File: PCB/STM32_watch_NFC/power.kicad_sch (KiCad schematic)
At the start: 26 parts, among them P1 USB_C_Plug_USB2.0, Q2 AO3400A, U4 LP5912-3.3DRV, U5 MCP73831-3-OT, U6 MT3608

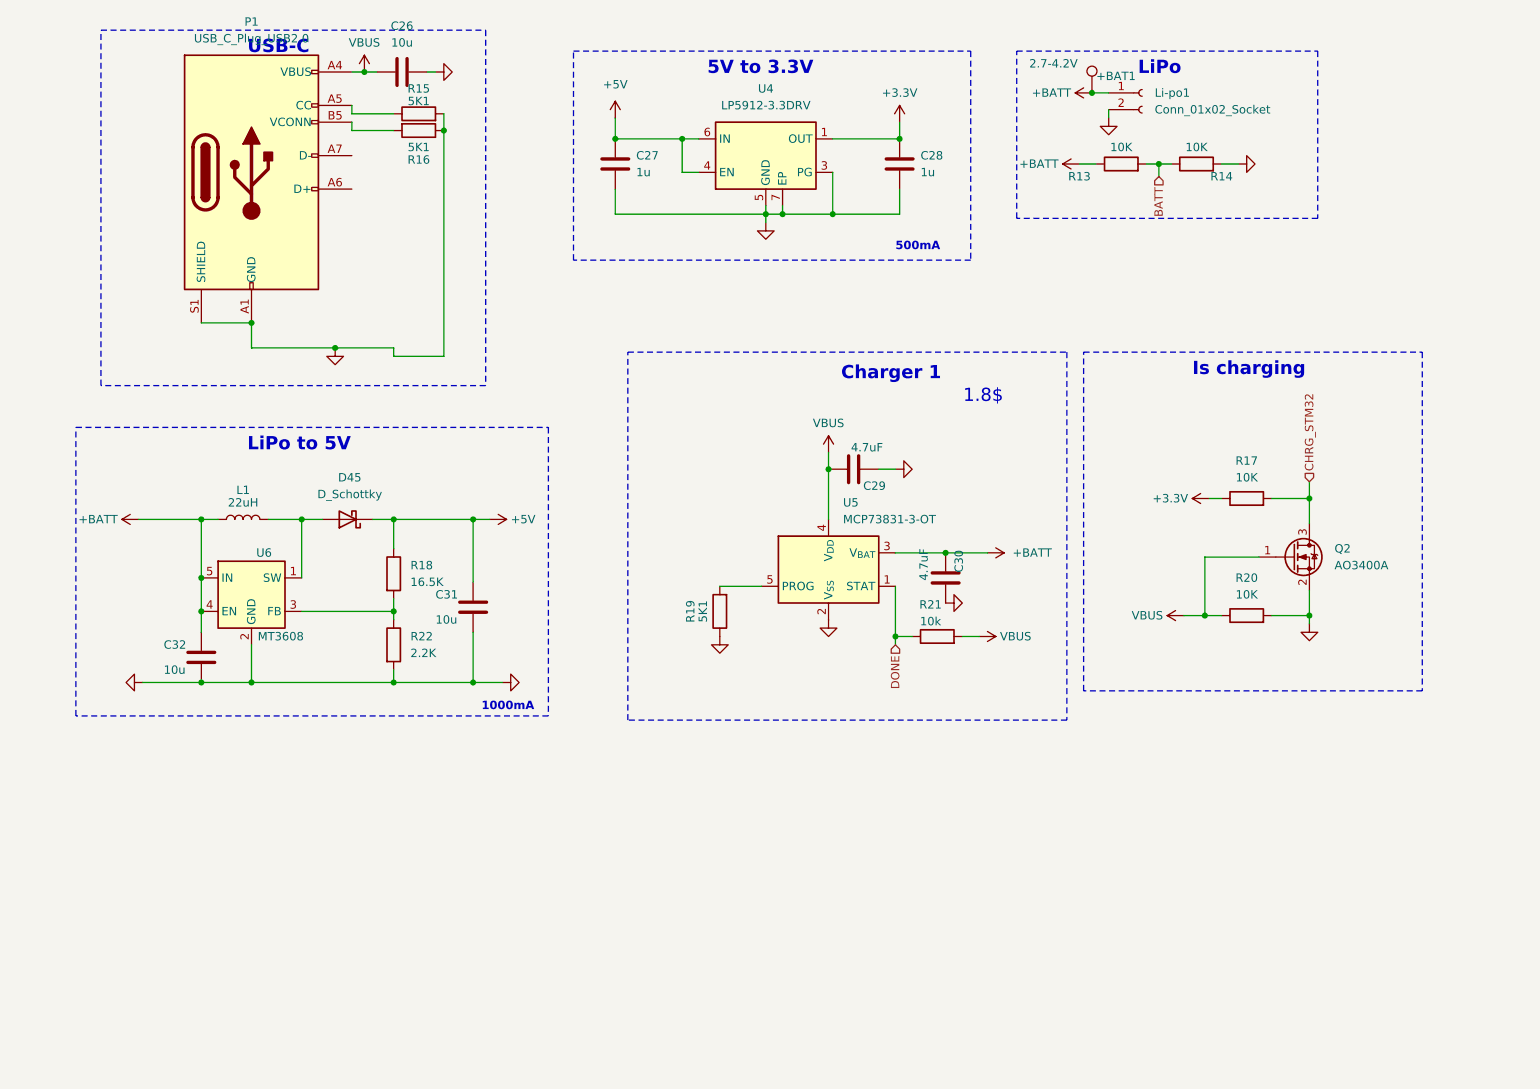
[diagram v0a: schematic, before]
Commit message: Whole power schema
I draw the whole power section and I am starting to create accelerometer with gyro
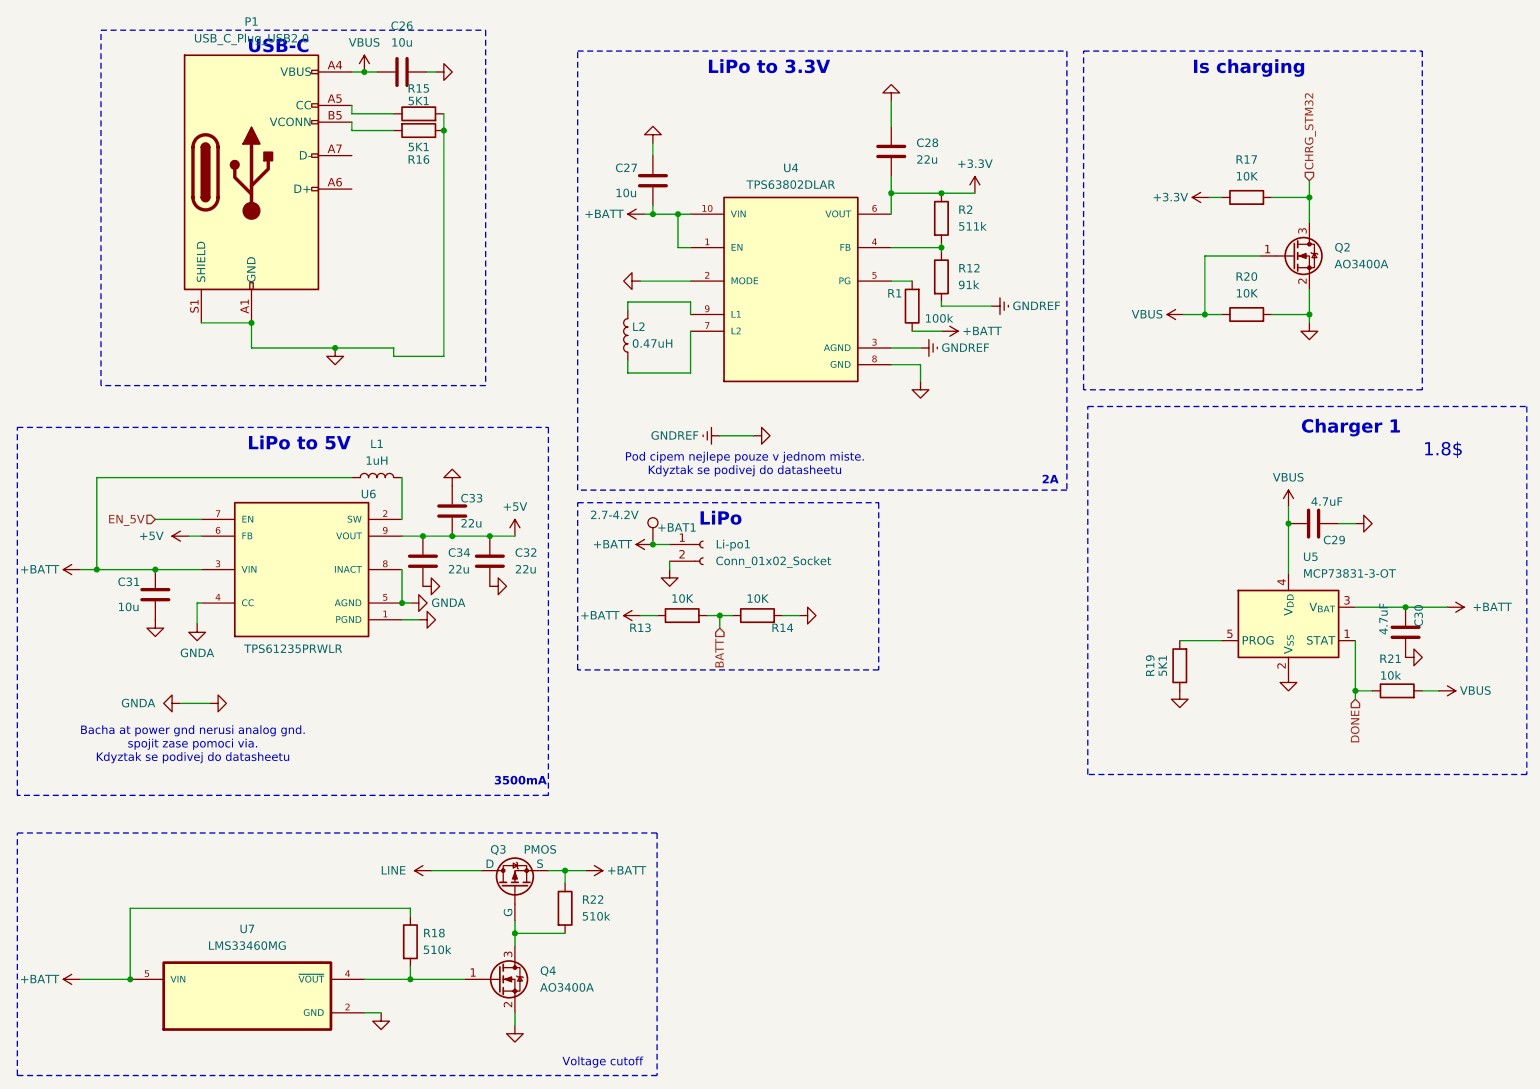
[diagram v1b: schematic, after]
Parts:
- removed D45: D_Schottky, Diode_SMD:D_SOD-523, symbol Device:D_Schottky
- removed U4: LP5912-3.3DRV, Package_SON:WSON-6-1EP_2x2mm_P0.65mm_EP1x1.6mm, symbol Regulator_Linear:LP5912-3.3DRV
- removed U6: MT3608, Package_TO_SOT_SMD:SOT-23-6, symbol Regulator_Switching:MT3608
- added C33, C34: 22u, symbol Device:C
- added L2: 0.47uH, symbol Device:L
- added Q3: PMOS, symbol Simulation_SPICE:PMOS
- added Q4: AO3400A, Package_TO_SOT_SMD:SOT-23, symbol Transistor_FET:AO3400A
- added R1: 100k, symbol Device:R
- added R12: 91k, symbol Device:R
- added R2: 511k, symbol Device:R
- added U4: TPS63802DLAR, TPS63802DLAR:VREG_TPS63802DLAR, symbol TPS63802DLAR:TPS63802DLAR
- added U6: TPS61235PRWLR, TPS61235PRWLR:CONV_TPS61235PRWLR, symbol TPS61235PRWLR:TPS61235PRWLR
- added U7: LMS33460MG, LMS33460MG:SOT65P210X110-5N, symbol LMS33460MG:LMS33460MG
- C27: value 1u -> 10u; footprint Capacitor_SMD:C_0402_1005Metric -> Capacitor_SMD:C_0603_1608Metric; LCSC C52923 -> C19702
- C28: value 1u -> 22u; footprint Capacitor_SMD:C_0402_1005Metric -> (none); LCSC C52923 -> (none)
- C32: value 10u -> 22u; footprint Capacitor_SMD:C_0603_1608Metric -> (none); LCSC C19702 -> (none)
- L1: value 22uH -> 1uH; footprint Inductor_SMD:L_Sunlord_SWPA3015S -> (none); LCSC C167761 -> (none)
- R18: value 16.5K -> 510k; footprint Resistor_SMD:R_0805_2012Metric -> (none); LCSC C104028 -> (none)
- R22: value 2.2K -> 510k; footprint Resistor_SMD:R_0402_1005Metric -> (none); LCSC C25879 -> (none)
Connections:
- net +3.3V: now also R2.1, U4.6 (VOUT)
- net +5V: now also C32.1, C33.2, C34.1, U6.6 (FB), U6.9 (VOUT); no longer C27.2, C31.1, R18.1
- net +BATT: now also C27.2, C31.1, R18.1, R22.1, Q3.3 (S), R1.1, U4.1 (EN), U4.10 (VIN), U6.3 (VIN), U7.5 (VIN); no longer C32.1
- net GND: now also C33.1, C34.2, Q4.2 (S), R12.2, U4.2 (MODE), U4.3 (AGND), U4.8 (GND), U6.1 (PGND), U6.4 (CC), U6.5 (AGND), U6.8 (INACT), U7.2 (GND), U7.3 (GND); no longer R22.2
- net at R18.2: now also Q4.1 (G), U7.4 (~{VOUT}); no longer R22.1
- net at L1.2: now also U6.2 (SW)
- new net: R12.1, R2.2, U4.4 (FB)
- new net: Q3.2 (G), Q4.3 (D), R22.2
- new net: L2.1, U4.7 (L2)
- new net: L2.2, U4.9 (L1)
- new net: R1.2, U4.5 (PG)
- new net EN_5V: U6.7 (EN)
- new net LINE: Q3.1 (D)
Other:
- note added: "2A"
- note added: "3500mA"
- note added: "Bacha at power gnd nerusi analog gnd. spojit zase pomoci via. Kdyztak se podivej do datasheetu"
- note added: "LiPo to 3.3V"
- note added: "Pod cipem nejlepe pouze v jednom miste. Kdyztak se podivej do datasheetu"
- note added: "Voltage cutoff"
- note removed: "1000mA"
- note removed: "500mA"
- note removed: "5V to 3.3V"
- moved on the sheet: +BAT1, C29, C30, Li-po1, Q2, R13, R14, R17, R19, R20, R21, U5

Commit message: Schema done
I redraw some footprints and added accelerometer with gyro
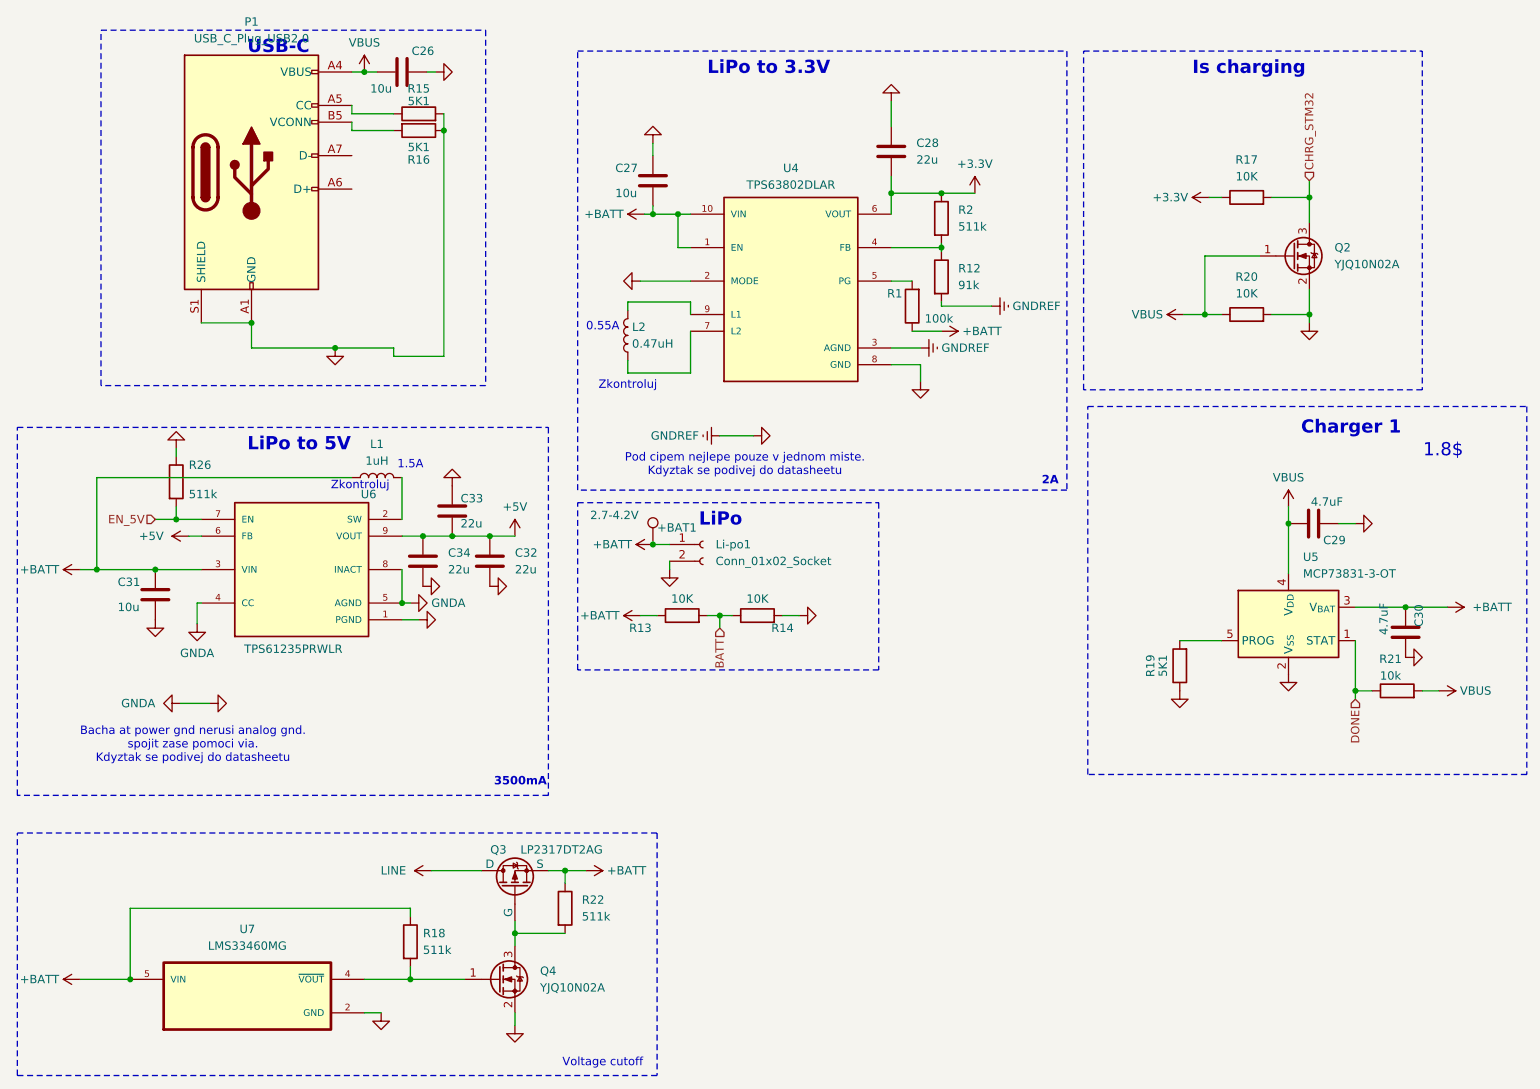
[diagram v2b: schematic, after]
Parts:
- added R26: 511k, Resistor_SMD:R_0603_1608Metric, symbol Device:R
- C28, C32, C33, C34: footprint (none) -> Capacitor_SMD:C_0603_1608Metric; LCSC (none) -> C59461
- L1: footprint (none) -> Inductor_SMD:L_1008_2520Metric; LCSC (none) -> C76795
- L2: footprint (none) -> Inductor_SMD:L_0805_2012Metric; LCSC (none) -> C370012
- Q2, Q4: value AO3400A -> YJQ10N02A; footprint Package_TO_SOT_SMD:SOT-23 -> Package_DFN_QFN:Diodes_UDFN2020-6_Type-F; LCSCv C344010 -> C919558
- Q3: value PMOS -> LP2317DT2AG; footprint (none) -> Package_DFN_QFN:Diodes_UDFN2020-6_Type-F; LCSC (none) -> C383254
- R1: footprint (none) -> Resistor_SMD:R_0603_1608Metric; LCSC (none) -> C25803
- R12: footprint (none) -> Resistor_SMD:R_0603_1608Metric; LCSC (none) -> C2907077
- R18, R22: value 510k -> 511k; footprint (none) -> Resistor_SMD:R_0603_1608Metric; LCSC (none) -> C2930114
- R2: footprint (none) -> Resistor_SMD:R_0603_1608Metric; LCSC (none) -> C2930114
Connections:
- net EN_5V: now also R26.2
- net GND: now also R26.1
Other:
- note added: "0.55A"
- note added: "1.5A"
- note added: "Zkontroluj"

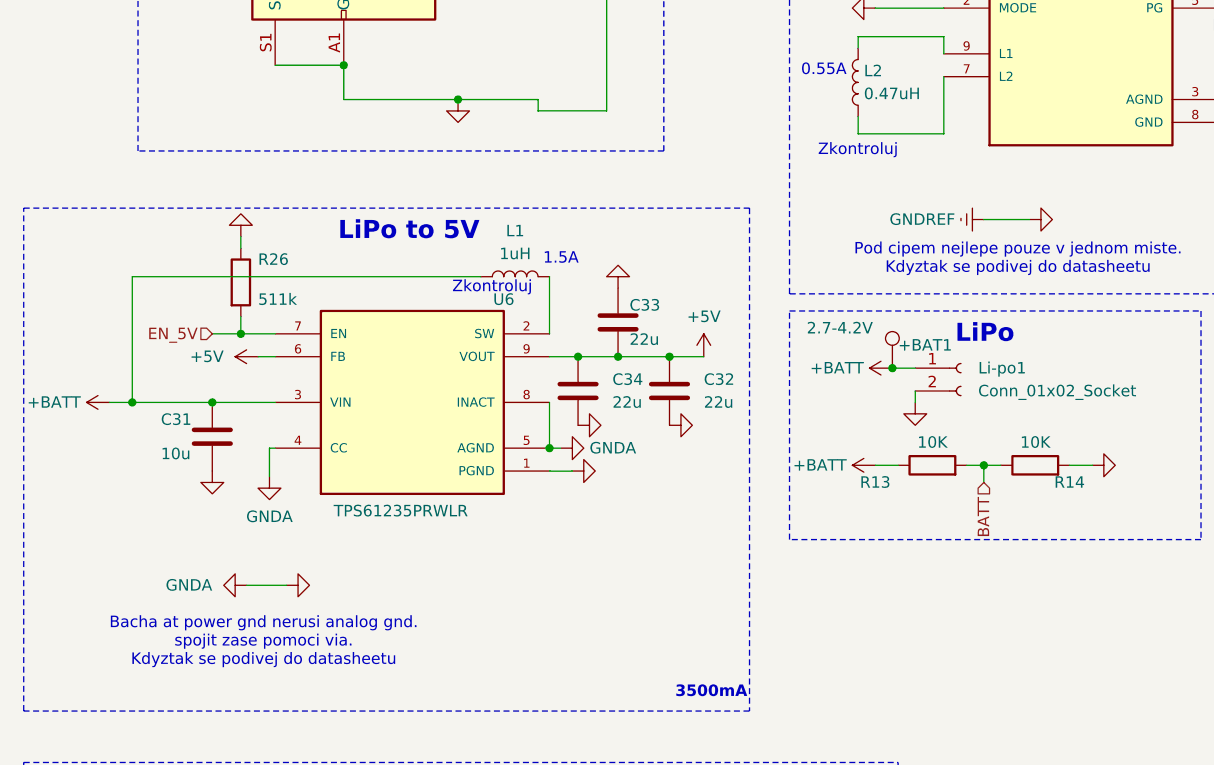
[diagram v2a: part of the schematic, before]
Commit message: PCB rev.B.1 #3
routing almost done - now checking and silkscreen
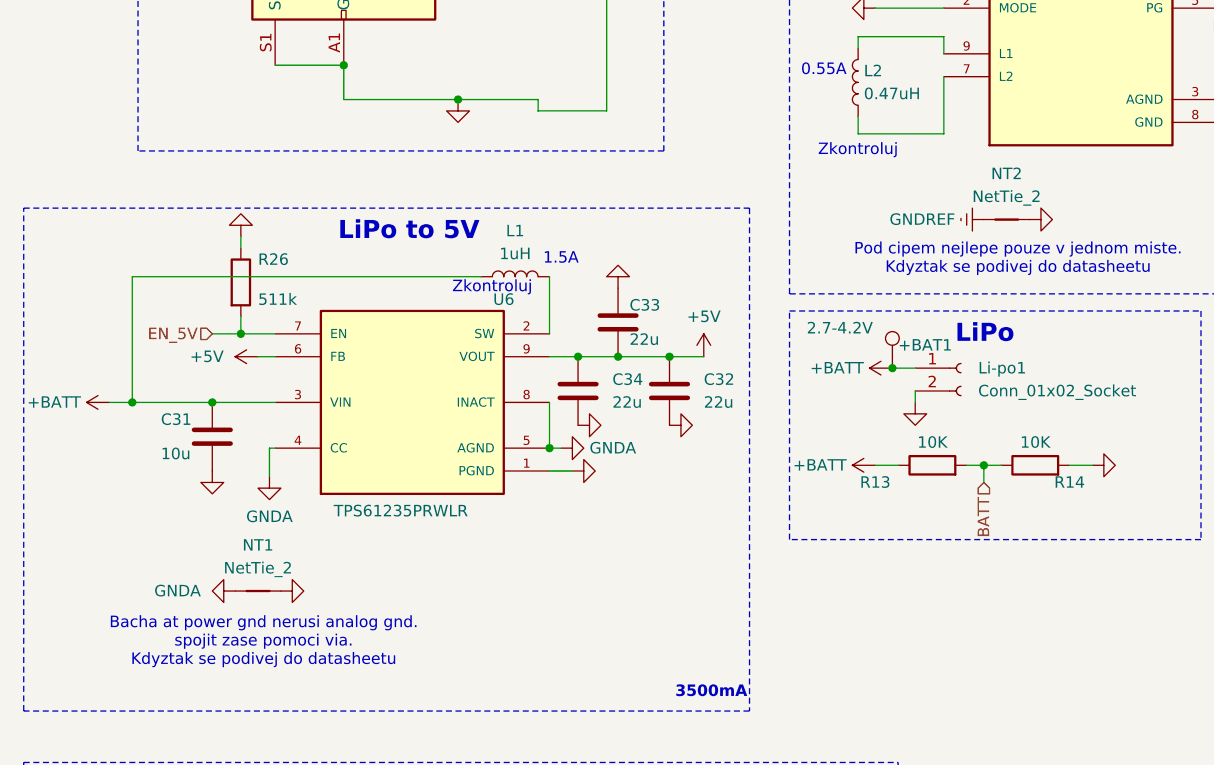
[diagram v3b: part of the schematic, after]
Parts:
- added NT1, NT2: NetTie_2, NetTie:NetTie-2_SMD_Pad0.5mm, symbol Device:NetTie_2
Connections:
- net GND: now also NT1.2, NT2.2; no longer R12.2, U4.3 (AGND), U6.4 (CC), U6.5 (AGND), U6.8 (INACT)
- new net GNDA: NT1.1, U6.4 (CC), U6.5 (AGND), U6.8 (INACT)
- new net GNDREF: NT2.1, R12.2, U4.3 (AGND)
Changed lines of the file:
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@@
 	(wire
 		(pts
-			(xy 39.37 123.19) (xy 43.815 123.19)
-		)
-		(stroke
-			(width 0)
-			(type default)
-		)
-	)
-	(wire
-		(pts
 			(xy 79.375 70.485) (xy 71.755 70.485)
 		)
@@
 	(wire
 		(pts
-			(xy 121.285 82.55) (xy 126.365 82.55)
-		)
-		(stroke
-			(width 0)
-			(type default)
-		)
-	)
-	(wire
-		(pts
 			(xy 195.58 46.355) (xy 197.485 46.355)
 		)
@@
 	)
 	(symbol
+		(lib_id "Device:NetTie_2")
+		(at 123.825 82.55 0)
+		(unit 1)
+		(exclude_from_sim no)
+		(in_bom no)
+		(on_board yes)
+		(dnp no)
+		(fields_autoplaced yes)
+		(property "Reference" "NT2"
+			(at 123.825 77.47 0)
+			(effects
+				(font
+					(size 1.27 1.27)
+				)
+			)
+		)
+		(property "Value" "NetTie_2"
+			(at 123.825 80.01 0)
+			(effects
+				(font
+					(size 1.27 1.27)
+				)
+			)
+		)
+		(property "Footprint" "NetTie:NetTie-2_SMD_Pad0.5mm"
+			(at 123.825 82.55 0)
+			(effects
+				(font
+					(size 1.27 1.27)
+				)
+				(hide yes)
+			)
+		)
+		(property "Datasheet" "~"
+			(at 123.825 82.55 0)
+			(effects
+				(font
+					(size 1.27 1.27)
+				)
+				(hide yes)
+			)
+		)
+		(property "Description" "Net tie, 2 pins"
+			(at 123.825 82.55 0)
+			(effects
+				(font
+					(size 1.27 1.27)
+				)
+				(hide yes)
+			)
+		)
+		(pin "2"
+		)
+		(pin "1"
+		)
+		(instances
+			(project "STM32_watch_NFC"
+				(path "/e445874f-c7a3-43dd-b930-6bce1d4fa2ef/d8aa51ff-304a-4e1d-85d0-2fbe17bc154e"
+					(reference "NT2")
+					(unit 1)
+				)
+			)
+		)
+	)
+	(symbol
 		(lib_id "LMS33460MG:LMS33460MG")
 		(at 49.53 167.64 0)
@@
 	(symbol
 		(lib_id "power:GNDA")
-		(at 39.37 123.19 270)
+		(at 38.1 123.825 270)
 		(unit 1)
 		(exclude_from_sim no)
@@
 		(fields_autoplaced yes)
 		(property "Reference" "#PWR0103"
-			(at 33.02 123.19 0)
+			(at 31.75 123.825 0)
 			(effects
 				(font
@@
 		)
 		(property "Value" "GNDA"
-			(at 35.56 123.1899 90)
+			(at 34.29 123.8249 90)
 			(effects
 				(font
@@
 		)
 		(property "Footprint" ""
-			(at 39.37 123.19 0)
+			(at 38.1 123.825 0)
 			(effects
 				(font
@@
 		)
 		(property "Datasheet" ""
-			(at 39.37 123.19 0)
+			(at 38.1 123.825 0)
 			(effects
 				(font
@@
 		)
 		(property "Description" "Power symbol creates a global label with name \"GNDA\" , analog ground"
-			(at 39.37 123.19 0)
+			(at 38.1 123.825 0)
 			(effects
 				(font
@@
 	(symbol
 		(lib_id "power:GND")
-		(at 43.815 123.19 90)
+		(at 43.18 123.825 90)
 		(unit 1)
 		(exclude_from_sim no)
@@
 		(fields_autoplaced yes)
 		(property "Reference" "#PWR0104"
-			(at 50.165 123.19 0)
+			(at 49.53 123.825 0)
 			(effects
 				(font
@@
 		)
 		(property "Value" "GND"
-			(at 48.895 123.19 0)
+			(at 48.26 123.825 0)
 			(effects
 				(font
@@
 		)
 		(property "Footprint" ""
-			(at 43.815 123.19 0)
+			(at 43.18 123.825 0)
 			(effects
 				(font
@@
 		)
 		(property "Datasheet" ""
-			(at 43.815 123.19 0)
+			(at 43.18 123.825 0)
 			(effects
 				(font
@@
 		)
 		(property "Description" ""
-			(at 43.815 123.19 0)
+			(at 43.18 123.825 0)
 			(effects
 				(font
@@
 					(unit 1)
 				)
+			)
+		)
+	)
+	(symbol
+		(lib_id "Device:NetTie_2")
+		(at 40.64 123.825 0)
+		(unit 1)
+		(exclude_from_sim no)
+		(in_bom no)
+		(on_board yes)
+		(dnp no)
+		(fields_autoplaced yes)
+		(property "Reference" "NT1"
+			(at 40.64 118.745 0)
+			(effects
+				(font
+					(size 1.27 1.27)
+				)
+			)
+		)
+		(property "Value" "NetTie_2"
+			(at 40.64 121.285 0)
+			(effects
+				(font
+					(size 1.27 1.27)
+				)
+			)
+		)
+		(property "Footprint" "NetTie:NetTie-2_SMD_Pad0.5mm"
+			(at 40.64 123.825 0)
+			(effects
+				(font
+					(size 1.27 1.27)
+				)
+				(hide yes)
+			)
+		)
+		(property "Datasheet" "~"
+			(at 40.64 123.825 0)
+			(effects
+				(font
+					(size 1.27 1.27)
+				)
+				(hide yes)
+			)
+		)
+		(property "Description" "Net tie, 2 pins"
+			(at 40.64 123.825 0)
+			(effects
+				(font
+					(size 1.27 1.27)
+				)
+				(hide yes)
+			)
+		)
+		(pin "2"
+		)
+		(pin "1"
+		)
+		(instances
+			(project ""
+				(path "/e445874f-c7a3-43dd-b930-6bce1d4fa2ef/d8aa51ff-304a-4e1d-85d0-2fbe17bc154e"
+					(reference "NT1")
+					(unit 1)
+				)
